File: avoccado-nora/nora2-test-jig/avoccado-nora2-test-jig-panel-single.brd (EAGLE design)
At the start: 25 x 25 mm, 24 parts

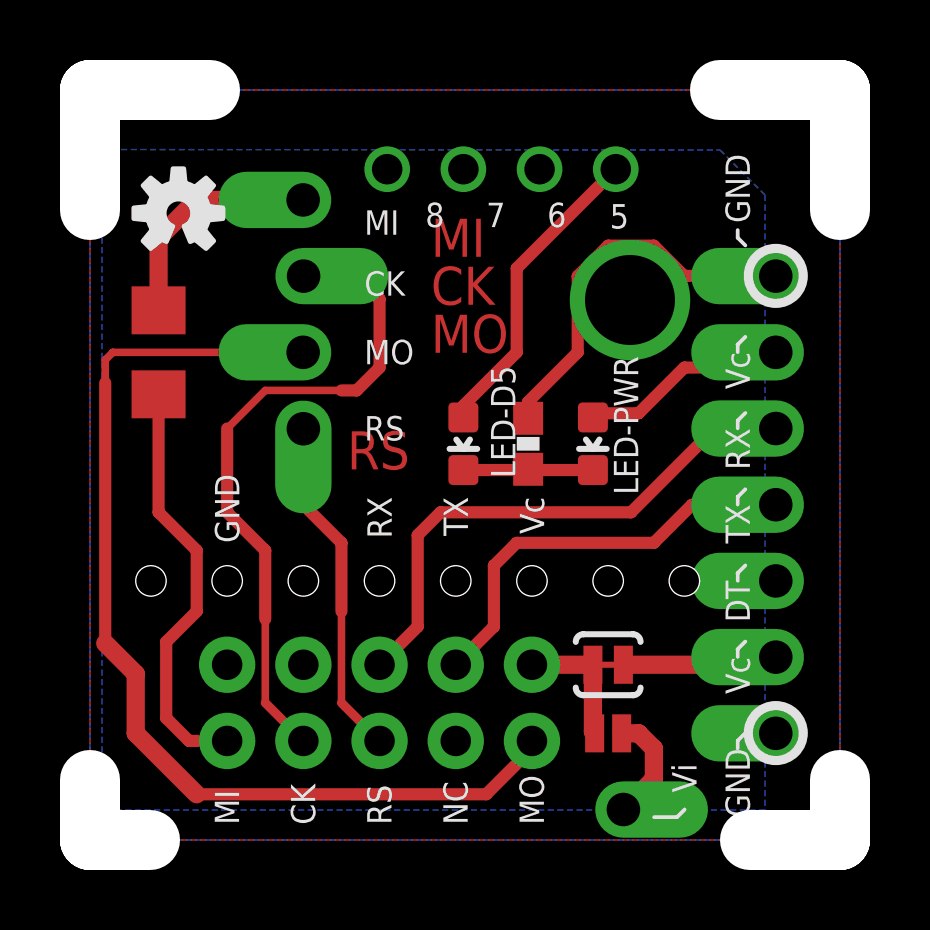
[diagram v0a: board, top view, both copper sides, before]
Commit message: bigger pads for test jig, g-code for solder stencils
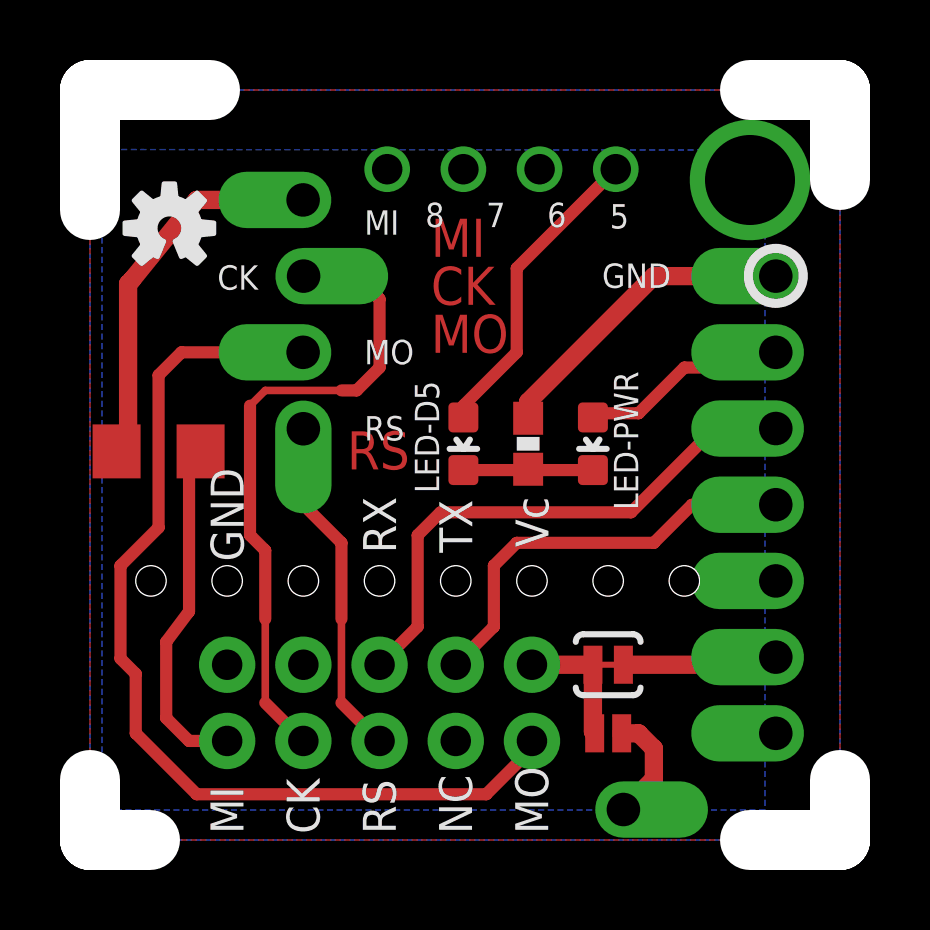
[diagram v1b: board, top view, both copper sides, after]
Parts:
- moved R1 3.30 mm to (2.29, 13.0), turned to 0 degrees
- moved LOGO2 0.58 mm to (2.65, 20.4)
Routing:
- net MISO: track 7.75 -> 12.9 mm
- net MISO1: track 14.1 -> 11.6 mm
- net GND: track 12.9 -> 10.5 mm
- net MOSI: track 34.5 -> 32.7 mm
- net SCK: track 22.5 -> 21.9 mm
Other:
- outline, holes or cut-outs redrawn
